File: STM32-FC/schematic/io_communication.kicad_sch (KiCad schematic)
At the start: 25 parts, among them J10 GH 1.25mm 6P, J11 GH 1.25mm 6P, J12 GH 1.25mm 6P, J13 GH 1.25mm 6P, J14 GH 1.25mm 4P, J15 GH 1.25mm 4P, J16 GH 1.25mm 4P, U12 ATA6561-GBQW, U13 ATA6561-GBQW

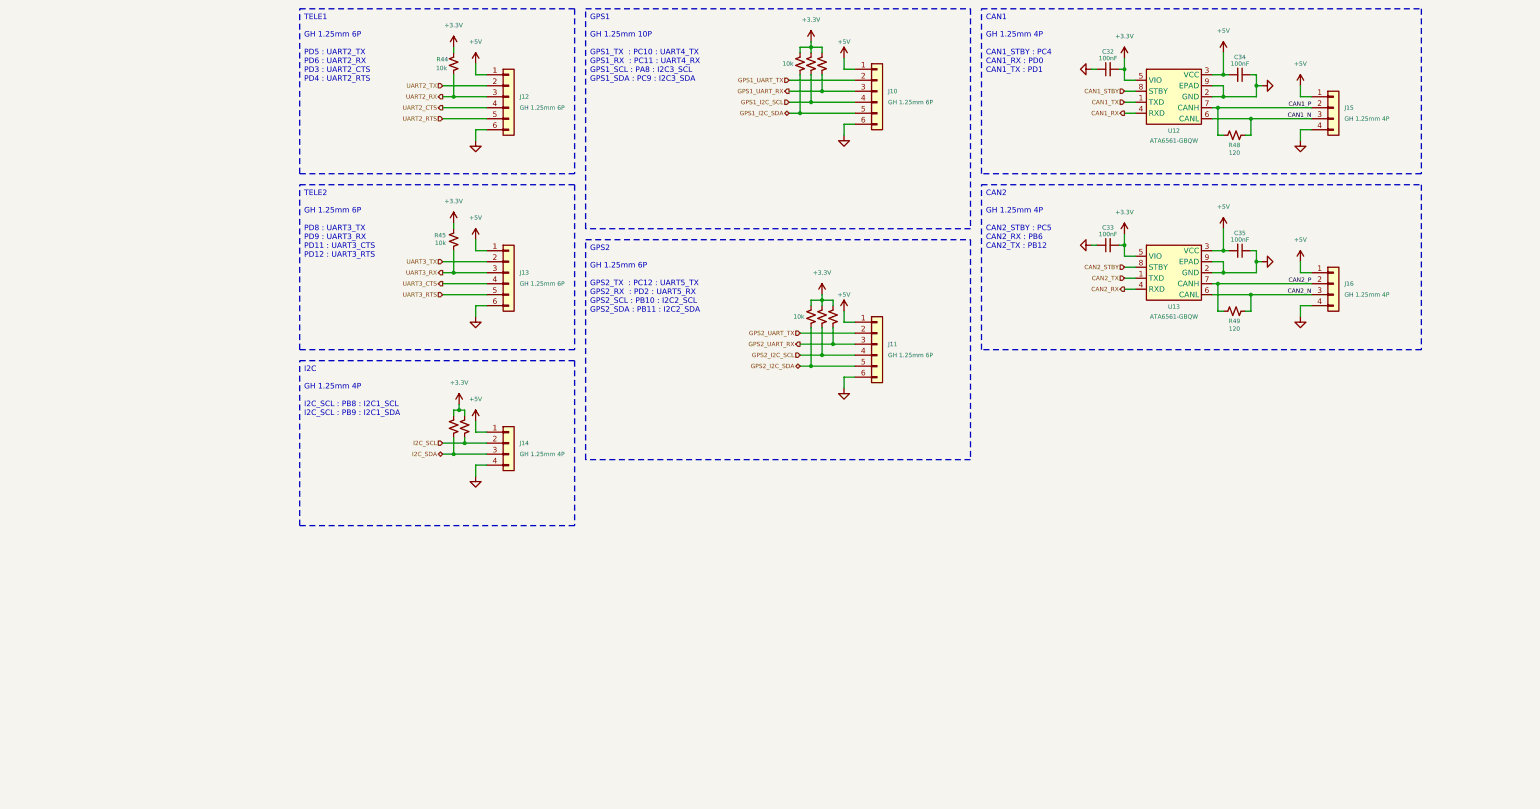
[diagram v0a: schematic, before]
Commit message: add basic circuit stm32f7
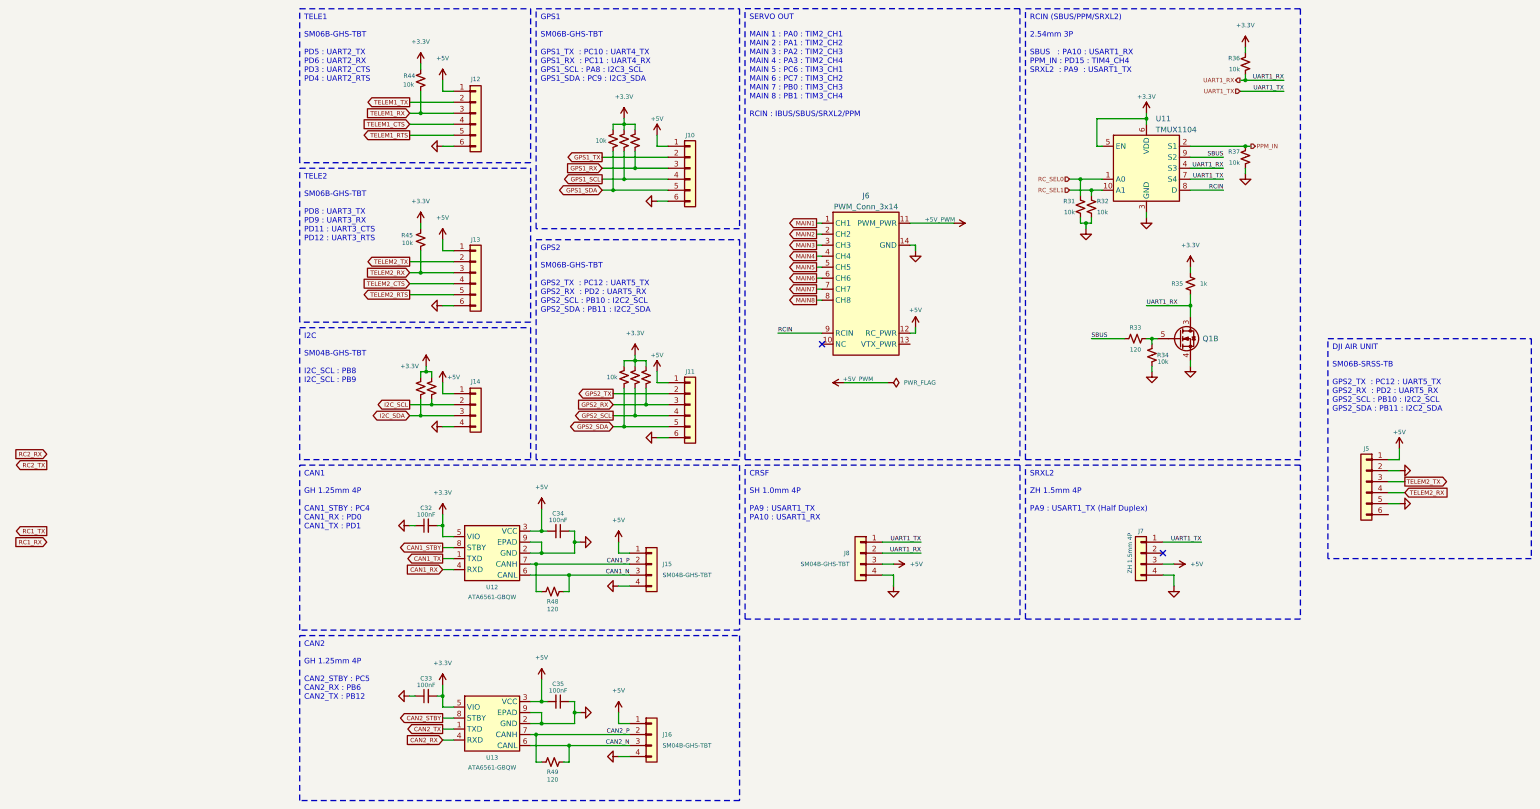
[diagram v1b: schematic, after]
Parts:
- added J5: SM06B-GHS-TBT, JST_GH:JST_GH_SM06B-GHS-TB_06x1.25mm_Angled, symbol Connector_Generic:Conn_01x06
- added J6: PWM_Conn_3x14, PWM_Connector:PWM_Conn_3x14, symbol PWM_Connector:PWM_Conn_3x10
- added J7: ZH 1.5mm 4P, JST_ZH:JST_ZH_S4B-ZR-SM4A-TF_1x04-1MP_P1.50mm_Horizontal, symbol Connector_Generic:Conn_01x04
- added J8: SM04B-GHS-TBT, JST_GH:JST_GH_SM04B-GHS-TB_04x1.25mm_Angled, symbol Connector_Generic:Conn_01x04
- added Q1: PMDPB30XN, Nexperia_SOT1118:Nexperia_SOT1118, symbol Nexperia_PMD:PMDPB30XN
- added R31, R32, R34, R36, R37: 10k, Resistor_SMD:R_0402_1005Metric, symbol Device:R_Small_US
- added R33: 120, Resistor_SMD:R_0402_1005Metric, symbol Device:R_Small_US
- added R35: 1k, Resistor_SMD:R_0402_1005Metric, symbol Device:R_Small_US
- added U11: TMUX1104, Package_SON:USON-10_2.5x1.0mm_P0.5mm, symbol TMUX1104:TMUX1104
- J10, J11, J12, J13: value GH 1.25mm 6P -> SM06B-GHS-TBT
- J14, J15, J16: value GH 1.25mm 4P -> SM04B-GHS-TBT
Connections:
- net +3.3V: now also R35.1, R36.1, U11.5 (EN), U11.6 (VDD)
- net +5V: now also J5.1 (Pin_1), J6.12 (RC_PWR), J7.3 (Pin_3), J8.3 (Pin_3)
- net GND: now also J5.2 (Pin_2), J5.5 (Pin_5), J6.14 (GND), J7.4 (Pin_4), J8.4 (Pin_4), Q1.4 (S), R31.2, R32.2, R34.2, R37.2, U11.3 (GND)
- net GPS1_I2C_SCL renamed GPS1_SCL
- net GPS1_I2C_SDA renamed GPS1_SDA
- net GPS1_UART_RX renamed GPS1_RX
- net GPS1_UART_TX renamed GPS1_TX
- net GPS2_I2C_SCL renamed GPS2_SCL
- net GPS2_I2C_SDA renamed GPS2_SDA
- net GPS2_UART_RX renamed GPS2_RX
- net GPS2_UART_TX renamed GPS2_TX
- net UART2_CTS renamed TELEM1_CTS
- net UART2_RTS renamed TELEM1_RTS
- net UART2_RX renamed TELEM1_RX
- net UART2_TX renamed TELEM1_TX
- net UART3_CTS renamed TELEM2_CTS
- net UART3_RTS renamed TELEM2_RTS
- net UART3_RX renamed TELEM2_RX
- net TELEM2_RX: now also J5.4 (Pin_4)
- net UART3_TX renamed TELEM2_TX
- net TELEM2_TX: now also J5.3 (Pin_3)
- new net: Q1.5 (G), R33.2, R34.1
- new net +5V_PWM: J6.11 (PWM_PWR)
- new net MAIN1: J6.1 (CH1)
- new net MAIN2: J6.2 (CH2)
- new net MAIN3: J6.3 (CH3)
- new net MAIN4: J6.4 (CH4)
- new net MAIN5: J6.5 (CH5)
- new net MAIN6: J6.6 (CH6)
- new net MAIN7: J6.7 (CH7)
- new net MAIN8: J6.8 (CH8)
- new net PPM_IN: R37.1, U11.2 (S1)
- new net RCIN: J6.9 (RCIN), U11.8 (D)
- new net RC_SEL0: R31.1, U11.1 (A0)
- new net RC_SEL1: R32.1, U11.10 (A1)
- new net SBUS: R33.1, U11.9 (S2)
- new net UART1_RX: J8.2 (Pin_2), Q1.3 (D), Q1.8 (D), R35.2, R36.2, U11.4 (S3)
- new net UART1_TX: J7.1 (Pin_1), J8.1 (Pin_1), U11.7 (S4)
- no-connect marks 0 -> 2
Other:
- note added: "2.54mm 3P SBUS : PA10 : USART1_RX PPM_IN : PD15 : TIM4_CH4 SRXL2 : PA9 : USART1_TX"
- note added: "CRSF"
- note added: "DJI AIR UNIT"
- note added: "MAIN 1 : PA0 : TIM2_CH1 MAIN 2 : PA1 : TIM2_CH2 MAIN 3 : PA2 : TIM2_CH3 MAIN 4 : PA3 : TIM2_CH4 MAIN 5 : PC6 : TIM3_CH1 MAIN 6 : PC7 : TIM3_CH2 MAIN 7 : PB0 : TIM3_CH3 MAIN 8 : PB1 : TIM3_CH4 RCIN : IBUS/SBUS/SRXL2/PPM"
- note added: "RCIN (SBUS/PPM/SRXL2)"
- note added: "SERVO OUT"
- note added: "SH 1.0mm 4P PA9 : USART1_TX PA10 : USART1_RX"
- note added: "SM04B-GHS-TBT I2C_SCL : PB8 I2C_SCL : PB9"
- note added: "SM06B-GHS-TBT GPS1_TX : PC10 : UART4_TX GPS1_RX : PC11 : UART4_RX GPS1_SCL : PA8 : I2C3_SCL GPS1_SDA : PC9 : I2C3_SDA"
- note added: "SM06B-GHS-TBT GPS2_TX : PC12 : UART5_TX GPS2_RX : PD2 : UART5_RX GPS2_SCL : PB10 : I2C2_SCL GPS2_SDA : PB11 : I2C2_SDA"
- note added: "SM06B-GHS-TBT PD5 : UART2_TX PD6 : UART2_RX PD3 : UART2_CTS PD4 : UART2_RTS"
- note added: "SM06B-GHS-TBT PD8 : UART3_TX PD9 : UART3_RX PD11 : UART3_CTS PD12 : UART3_RTS"
- note added: "SM06B-SRSS-TB GPS2_TX : PC12 : UART5_TX GPS2_RX : PD2 : UART5_RX GPS2_SCL : PB10 : I2C2_SCL GPS2_SDA : PB11 : I2C2_SDA"
- note added: "SRXL2"
- note added: "ZH 1.5mm 4P PA9 : USART1_TX (Half Duplex)"
- note removed: "GH 1.25mm 10P GPS1_TX : PC10 : UART4_TX GPS1_RX : PC11 : UART4_RX GPS1_SCL : PA8 : I2C3_SCL GPS1_SDA : PC9 : I2C3_SDA"
- note removed: "GH 1.25mm 4P I2C_SCL : PB8 : I2C1_SCL I2C_SCL : PB9 : I2C1_SDA"
- note removed: "GH 1.25mm 6P GPS2_TX : PC12 : UART5_TX GPS2_RX : PD2 : UART5_RX GPS2_SCL : PB10 : I2C2_SCL GPS2_SDA : PB11 : I2C2_SDA"
- note removed: "GH 1.25mm 6P PD5 : UART2_TX PD6 : UART2_RX PD3 : UART2_CTS PD4 : UART2_RTS"
- note removed: "GH 1.25mm 6P PD8 : UART3_TX PD9 : UART3_RX PD11 : UART3_CTS PD12 : UART3_RTS"
- moved on the sheet: C32, C33, C34, C35, J10, J11, J12, J13, J14, J15, J16, R44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

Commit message: add DJI Air unit and RC Selector
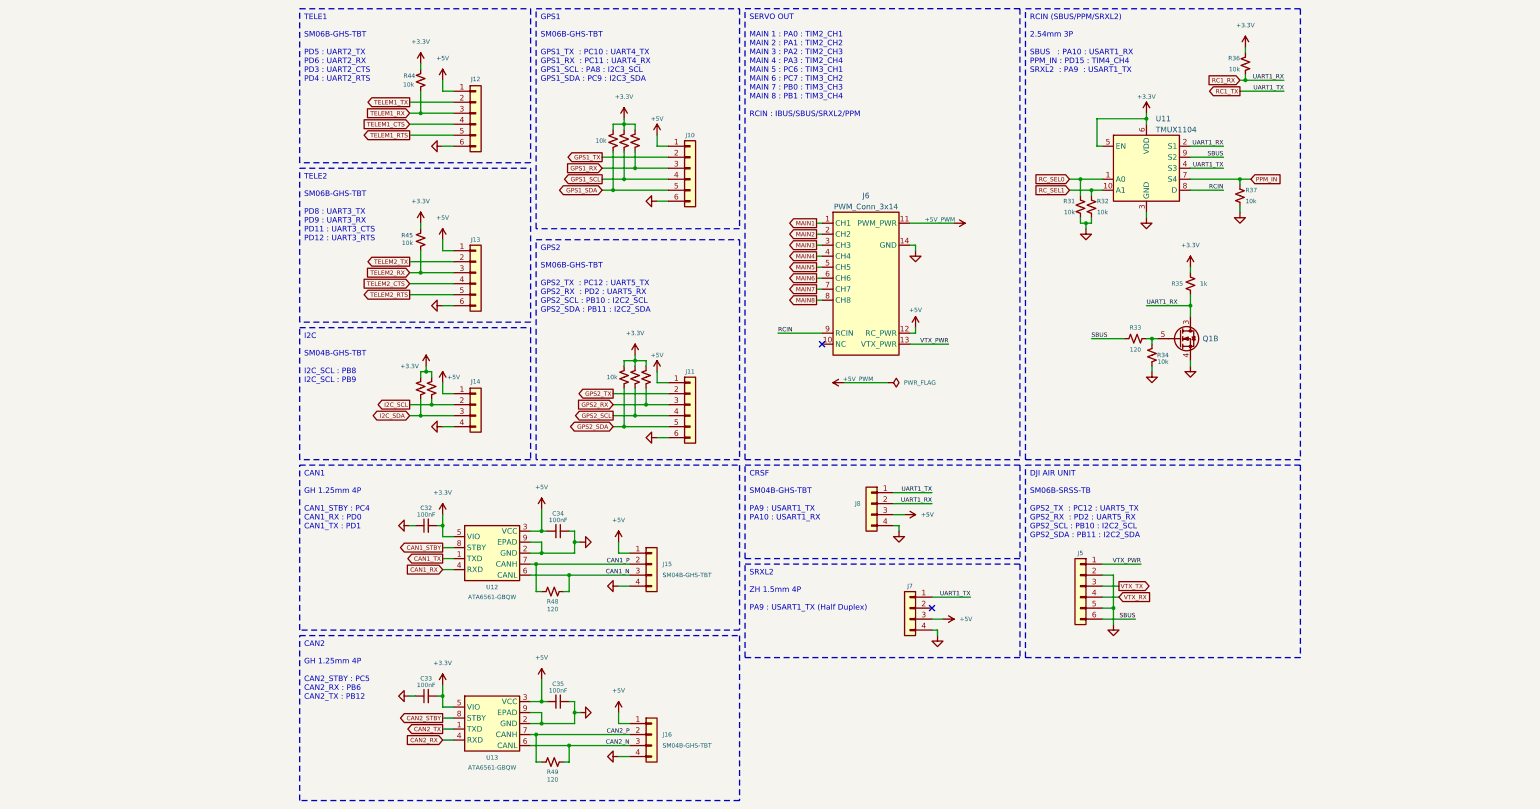
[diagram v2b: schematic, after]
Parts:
- J5: footprint JST_GH:JST_GH_SM06B-GHS-TB_06x1.25mm_Angled -> (none)
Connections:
- net +5V: no longer J5.1 (Pin_1)
- net PPM_IN: now also U11.7 (S4); no longer U11.2 (S1)
- net RC1_RX: now also J8.2 (Pin_2), Q1.3 (D), Q1.8 (D), R35.2, R36.2, U11.2 (S1)
- net RC1_TX: now also J7.1 (Pin_1), J8.1 (Pin_1), U11.4 (S3)
- net SBUS: now also J5.6 (Pin_6)
- net TELEM2_RX: no longer J5.4 (Pin_4)
- net TELEM2_TX: no longer J5.3 (Pin_3)
- net VTX_PWR: now reaches J6.13 (VTX_PWR)
- net VTX_PWR: now also J5.1 (Pin_1)
- removed net UART1_RX: J8.2 (Pin_2), Q1.3 (D), Q1.8 (D), R35.2, R36.2, U11.4 (S3)
- removed net UART1_TX: J7.1 (Pin_1), J8.1 (Pin_1), U11.7 (S4)
- new net VTX_RX: J5.4 (Pin_4)
- new net VTX_TX: J5.3 (Pin_3)
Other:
- note added: "SM04B-GHS-TBT PA9 : USART1_TX PA10 : USART1_RX"
- note removed: "SH 1.0mm 4P PA9 : USART1_TX PA10 : USART1_RX"
- moved on the sheet: J5, J7, J8, R37

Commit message: ERC passed
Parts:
- renumbered C32 to C49, C33 to C50, C34 to C51, C35 to C52, J6 to J12, J8 to J13, J7 to J14, J5 to J15, J12 to J5, J13 to J6, J14 to J7, J15 to J8, J16 to J9, R44 to R19, R45 to R20, R46 to R21, R47 to R22, R48 to R23, R49 to R24, R38 to R25, R39 to R26, R40 to R27, R41 to R28, R42 to R29, R43 to R30, R37 to R36, R36 to R37, U12 to U11, U13 to U12, U11 to U13
